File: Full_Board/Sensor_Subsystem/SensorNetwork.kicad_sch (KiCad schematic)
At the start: 0 parts

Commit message: Finalize MSP432, stepper, and button subsheets
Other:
- note added: "General Notes: This should be the entire sensor network We can do a subsheet for the individual reed witch components if needed"
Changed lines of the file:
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@@
     (company "The Great Gambit")
   )
+  (text "General Notes:\n	This should be the entire sensor network\n	We can do a subsheet for the individual reed witch components if needed"
+    (at 19.05 24.13 0)
+    (effects (font (size 1.27 1.27)) (justify left bottom))
+  )
 )

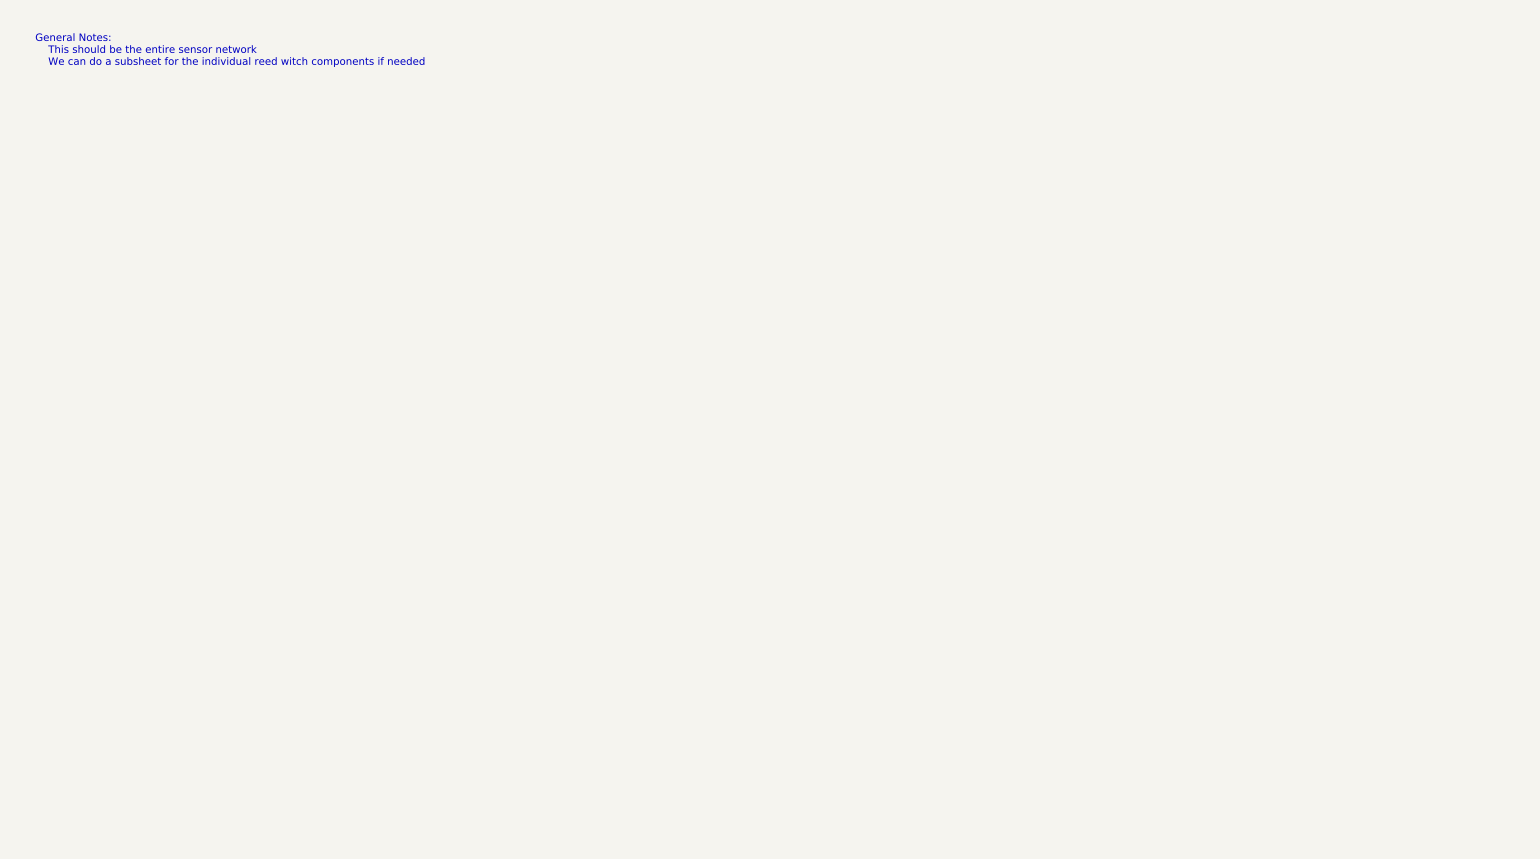
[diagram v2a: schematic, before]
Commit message: Merge Eli and Gabi files. Remove unecessary ECAD remnants. Update stepper components post-part order
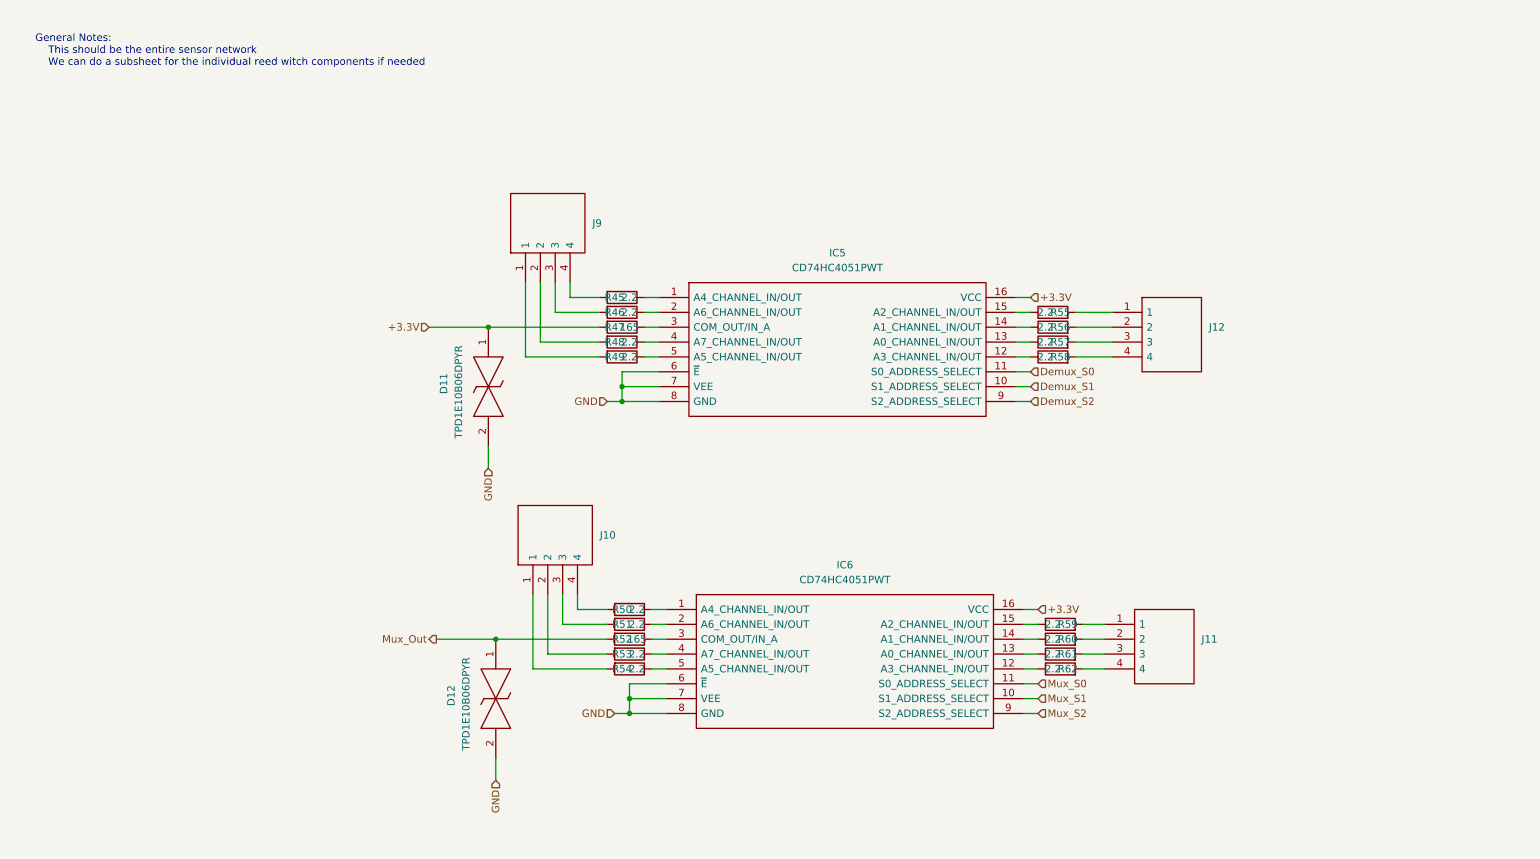
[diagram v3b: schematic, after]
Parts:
- added D11, D12: TPD1E10B06DPYR, TPD1E10B06DPYR:TPD1E10B06DPYR, symbol TPD1E10B06DPYR:TPD1E10B06DPYR
- added IC5, IC6: CD74HC4051PWT, SOP65P640X120-16N, symbol CD74HC4051PWT:CD74HC4051PWT
- added J10, J11, J12, J9: OQ0432500000G, OQ0432500000G:RHDR4W80P0X381_1X4_1540X700X920P, symbol OQ04325500000G:OQ0432500000G
- added R45, R46, R48, R49, R50, R51, R53, R54, R55, R56, R57, R58, R59, R60, R61, R62: 2.2, symbol Device:R
- added R47, R52: 165, symbol Device:R
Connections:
- new net: IC5.1 (A4_CHANNEL_IN/OUT), R45.1
- new net: J9.4, R45.2
- new net: IC6.1 (A4_CHANNEL_IN/OUT), R50.1
- new net: IC6.12 (A3_CHANNEL_IN/OUT), R62.1
- new net: IC6.13 (A0_CHANNEL_IN/OUT), R61.1
- new net: IC6.14 (A1_CHANNEL_IN/OUT), R60.1
- new net: IC6.15 (A2_CHANNEL_IN/OUT), R59.1
- new net: IC6.2 (A6_CHANNEL_IN/OUT), R51.1
- new net: IC6.3 (COM_OUT/IN_A), R52.1
- new net: IC6.4 (A7_CHANNEL_IN/OUT), R53.1
- new net: IC6.5 (A5_CHANNEL_IN/OUT), R54.1
- new net: J11.1, R59.2
- new net: J11.2, R60.2
- new net: J11.3, R61.2
- new net: J11.4, R62.2
- new net: J10.1, R54.2
- new net: J10.2, R53.2
- new net: J10.3, R51.2
- new net: J10.4, R50.2
- new net: IC5.5 (A5_CHANNEL_IN/OUT), R49.1
- new net: J9.1, R49.2
- new net: J12.1, R55.2
- new net: J12.2, R56.2
- new net: J12.3, R57.2
- new net: J12.4, R58.2
- new net: IC5.2 (A6_CHANNEL_IN/OUT), R46.1
- new net: J9.3, R46.2
- new net: IC5.4 (A7_CHANNEL_IN/OUT), R48.1
- new net: J9.2, R48.2
- new net: IC5.14 (A1_CHANNEL_IN/OUT), R56.1
- new net: IC5.13 (A0_CHANNEL_IN/OUT), R57.1
- new net: IC5.15 (A2_CHANNEL_IN/OUT), R55.1
- new net: IC5.12 (A3_CHANNEL_IN/OUT), R58.1
- new net: IC5.3 (COM_OUT/IN_A), R47.1
- new net +3.3V: D11.1, IC5.16 (VCC), IC6.16 (VCC), R47.2
- new net Demux_S0: IC5.11 (S0_ADDRESS_SELECT)
- new net Demux_S1: IC5.10 (S1_ADDRESS_SELECT)
- new net Demux_S2: IC5.9 (S2_ADDRESS_SELECT)
- new net GND: D11.2, D12.2, IC5.6 (~{E}), IC5.7 (VEE), IC5.8 (GND), IC6.6 (~{E}), IC6.7 (VEE), IC6.8 (GND)
- new net Mux_Out: D12.1, R52.2
- new net Mux_S0: IC6.11 (S0_ADDRESS_SELECT)
- new net Mux_S1: IC6.10 (S1_ADDRESS_SELECT)
- new net Mux_S2: IC6.9 (S2_ADDRESS_SELECT)

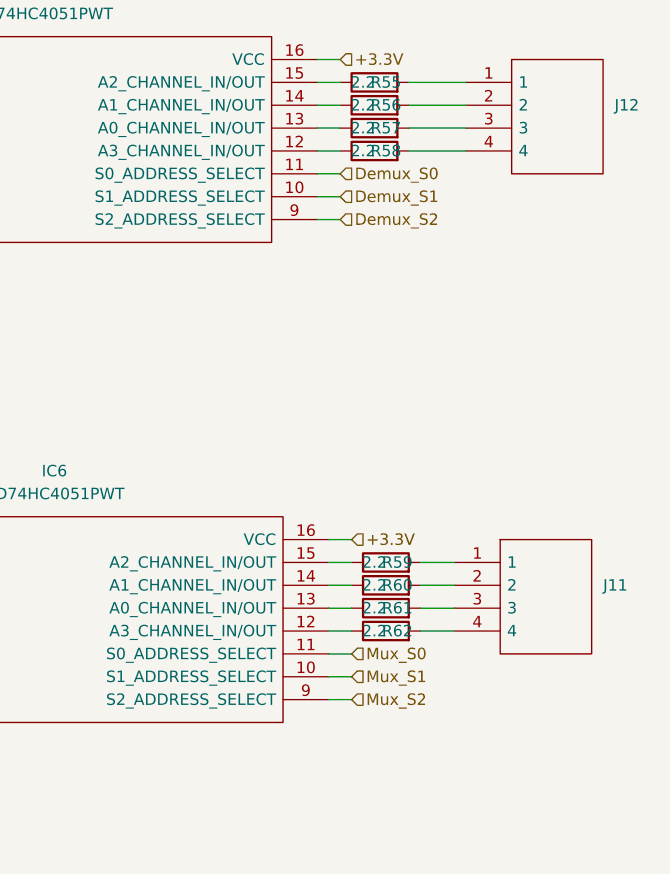
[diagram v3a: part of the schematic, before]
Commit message: Added a fuse and fixed ERC
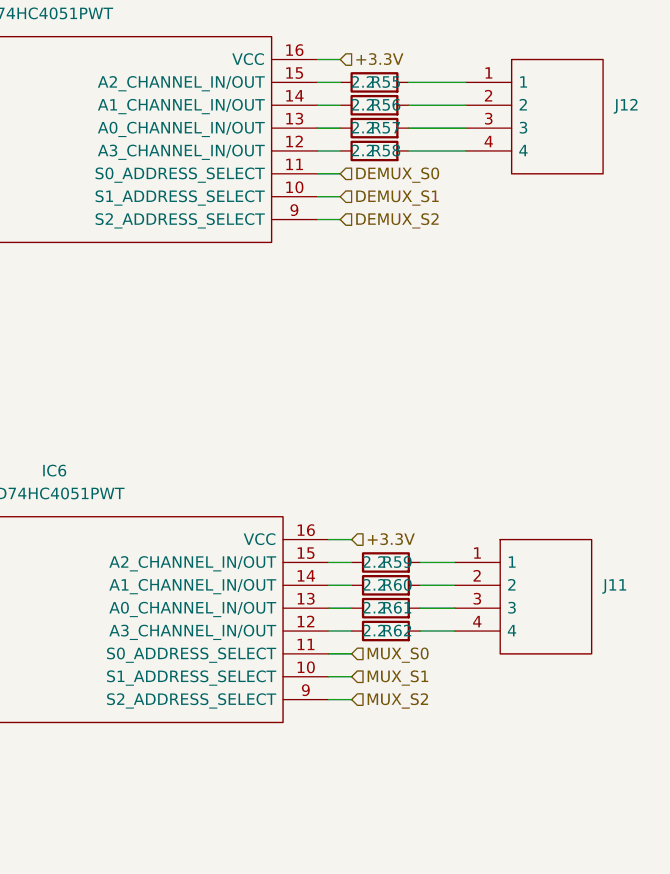
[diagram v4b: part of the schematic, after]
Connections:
- net Demux_S0 renamed DEMUX_S0
- net Demux_S1 renamed DEMUX_S1
- net Demux_S2 renamed DEMUX_S2
- net Mux_S0 renamed MUX_S0
- net Mux_S1 renamed MUX_S1
- net Mux_S2 renamed MUX_S2
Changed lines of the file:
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@@
     (effects (font (size 1.27 1.27)) (justify left bottom))
   )
-  (hierarchical_label "Demux_S0" (shape input) (at 189.23 76.2 0)
+  (hierarchical_label "DEMUX_S0" (shape input) (at 189.23 76.2 0)
     (effects (font (size 1.27 1.27)) (justify left))
   )
@@
     (effects (font (size 1.27 1.27)) (justify right))
   )
-  (hierarchical_label "Mux_S1" (shape input) (at 190.5 132.08 0)
+  (hierarchical_label "MUX_S1" (shape input) (at 190.5 132.08 0)
     (effects (font (size 1.27 1.27)) (justify left))
   )
-  (hierarchical_label "Demux_S2" (shape input) (at 189.23 81.28 0)
+  (hierarchical_label "DEMUX_S2" (shape input) (at 189.23 81.28 0)
     (effects (font (size 1.27 1.27)) (justify left))
   )
@@
     (effects (font (size 1.27 1.27)) (justify left))
   )
-  (hierarchical_label "Mux_S0" (shape input) (at 190.5 129.54 0)
+  (hierarchical_label "MUX_S0" (shape input) (at 190.5 129.54 0)
     (effects (font (size 1.27 1.27)) (justify left))
   )
@@
     (effects (font (size 1.27 1.27)) (justify right))
   )
-  (hierarchical_label "Demux_S1" (shape input) (at 189.23 78.74 0)
+  (hierarchical_label "DEMUX_S1" (shape input) (at 189.23 78.74 0)
     (effects (font (size 1.27 1.27)) (justify left))
   )
-  (hierarchical_label "Mux_S2" (shape input) (at 190.5 134.62 0)
+  (hierarchical_label "MUX_S2" (shape input) (at 190.5 134.62 0)
     (effects (font (size 1.27 1.27)) (justify left))
   )

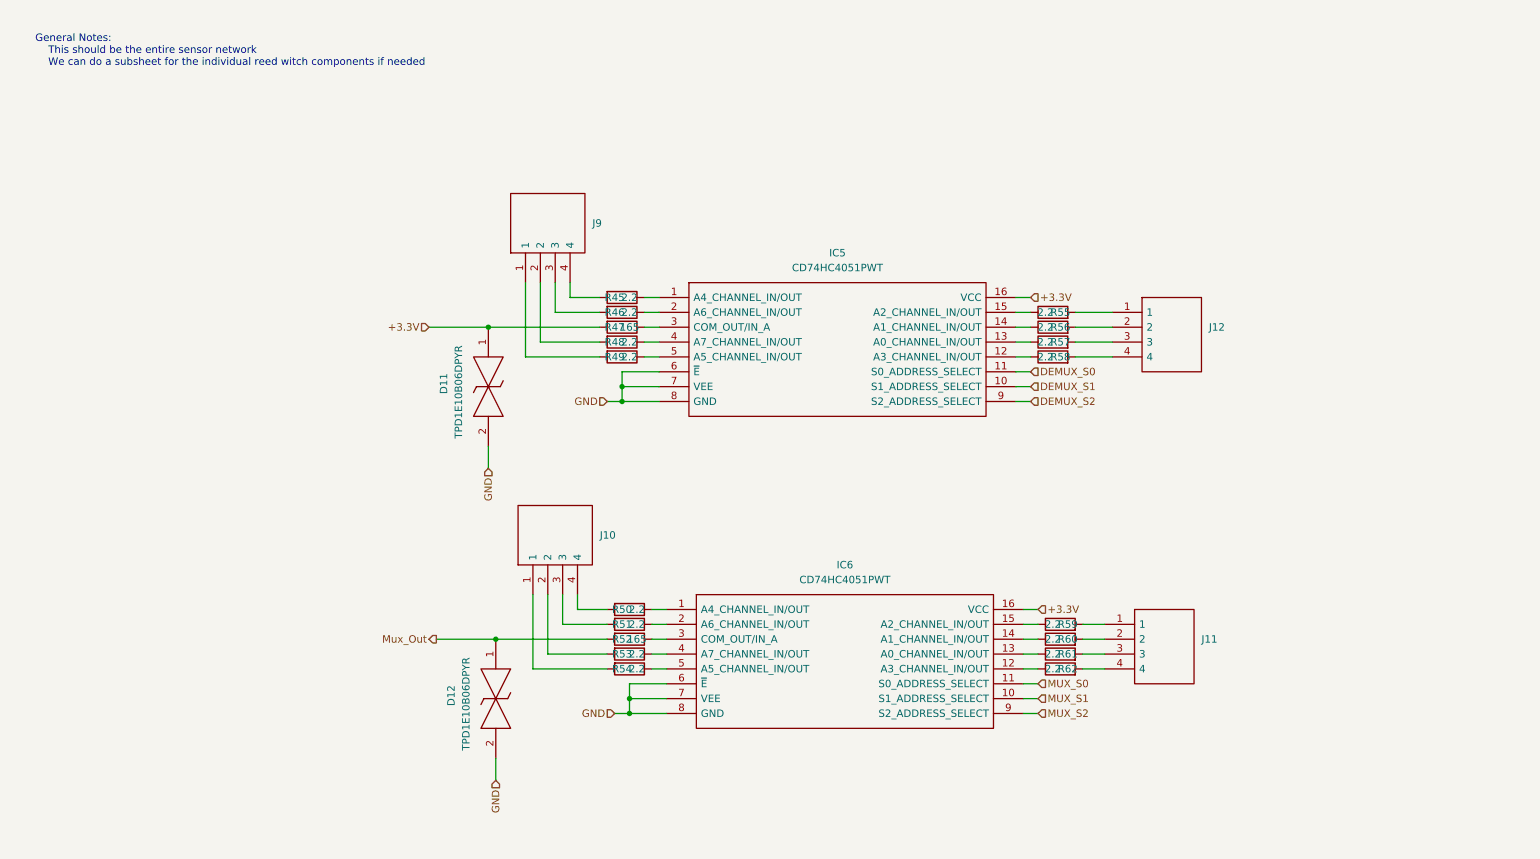
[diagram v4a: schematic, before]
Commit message: Redo sensor network, redo MSP432 connections, redo LED subsystem, add shunts throughout, ERC still passes
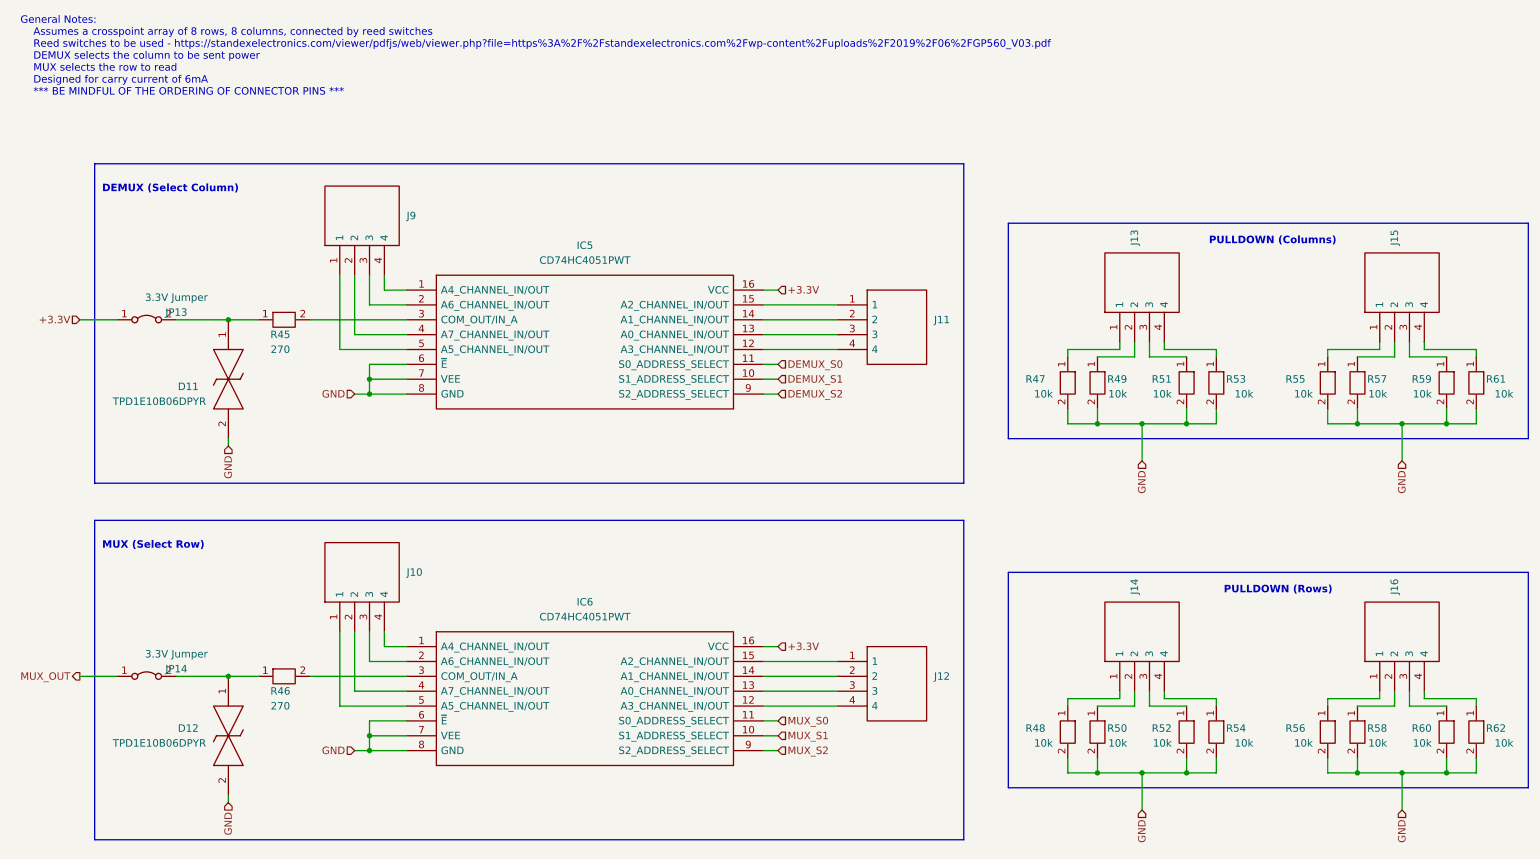
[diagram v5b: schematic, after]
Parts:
- removed R45, R46, R48, R49, R50, R51, R53, R54, R55, R56, R57, R58, R59, R60, R61, R62: 2.2, symbol Device:R
- removed R47, R52: 165, symbol Device:R
- added J13, J14, J15, J16: OQ0432500000G, OQ0432500000G:RHDR4W80P0X381_1X4_1540X700X920P, symbol OQ04325500000G:OQ0432500000G
- added JP13, JP14: 3.3V Jumper, TestPoint:TestPoint_2Pads_Pitch2.54mm_Drill0.8mm, symbol Jumper:Jumper_2_Bridged
- added R45, R46: 270, SDR10EZPJ271:RESC2012X65N, symbol SDR10EZPJ271:SDR10EZPJ271
- added R47, R48, R49, R50, R51, R52, R53, R54, R55, R56, R57, R58, R59, R60, R61, R62: 10k, RESC3225X74N, symbol RMCF1206FT10K0:10k
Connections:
- net +3.3V: now also JP13.1 (A); no longer D11.1
- net GND: now also R47.2, R48.2, R49.2, R50.2, R51.2, R52.2, R53.2, R54.2, R55.2, R56.2, R57.2, R58.2, R59.2, R60.2, R61.2, R62.2
- net at IC5.1 (A4_CHANNEL_IN/OUT): now also J9.4
- net at IC6.1 (A4_CHANNEL_IN/OUT): now also J10.4
- net at IC6.12 (A3_CHANNEL_IN/OUT): now also J12.4
- net at IC6.13 (A0_CHANNEL_IN/OUT): now also J12.3
- net at IC6.14 (A1_CHANNEL_IN/OUT): now also J12.2
- net at IC6.15 (A2_CHANNEL_IN/OUT): now also J12.1
- net at IC6.2 (A6_CHANNEL_IN/OUT): now also J10.3
- net at IC6.3 (COM_OUT/IN_A): now also R46.2
- net at IC6.4 (A7_CHANNEL_IN/OUT): now also J10.2
- net at IC6.5 (A5_CHANNEL_IN/OUT): now also J10.1
- net at J11.1: now also IC5.15 (A2_CHANNEL_IN/OUT)
- net at J11.2: now also IC5.14 (A1_CHANNEL_IN/OUT)
- net at J11.3: now also IC5.13 (A0_CHANNEL_IN/OUT)
- net at J11.4: now also IC5.12 (A3_CHANNEL_IN/OUT)
- net at IC5.5 (A5_CHANNEL_IN/OUT): now also J9.1
- net at IC5.2 (A6_CHANNEL_IN/OUT): now also J9.3
- net at IC5.4 (A7_CHANNEL_IN/OUT): now also J9.2
- net at IC5.3 (COM_OUT/IN_A): now also R45.2
- net Mux_Out: no longer names the net of D12.1
- net Mux_Out: now also JP14.2 (B), R46.1
- new net: J16.4, R62.1
- new net: J16.3, R60.1
- new net: D11.1, JP13.2 (B), R45.1
- new net: J15.3, R59.1
- new net: J13.1, R47.1
- new net: J14.2, R50.1
- new net: J13.3, R51.1
- new net: J15.4, R61.1
- new net: J13.4, R53.1
- new net: J15.2, R57.1
- new net: J14.3, R52.1
- new net: J16.1, R56.1
- new net: J16.2, R58.1
- new net: J13.2, R49.1
- new net: J14.1, R48.1
- new net: J14.4, R54.1
- new net: J15.1, R55.1
- new net MUX_OUT: JP14.1 (A)
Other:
- note added: "DEMUX (Select Column)"
- note added: "General Notes: Assumes a crosspoint array of 8 rows, 8 columns, connected by reed switches Reed switches to be used - https://standexelectronics.com/viewer/pdfjs/web/viewer.php?file=https%3A%2F%2Fstandexelectronics.com%2Fwp-content%2Fuploads%2F2019%2F06%2FGP560_V03.pdf DEMUX selects the column to be sent power MUX selects the row to read Designed for carry current of 6mA *** BE MINDFUL OF THE ORD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"
- note added: "MUX (Select Row)"
- note added: "PULLDOWN (Columns)"
- note added: "PULLDOWN (Rows)"
- note removed: "General Notes: This should be the entire sensor network We can do a subsheet for the individual reed witch components if needed"
- moved on the sheet: D11, IC5
